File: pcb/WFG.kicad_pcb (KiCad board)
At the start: 2 copper layers, 54.1 x 30.5 mm, 32 parts, among them J1 Conn_01x02_Pin, J2 Conn_01x04_Socket, U1 LM324

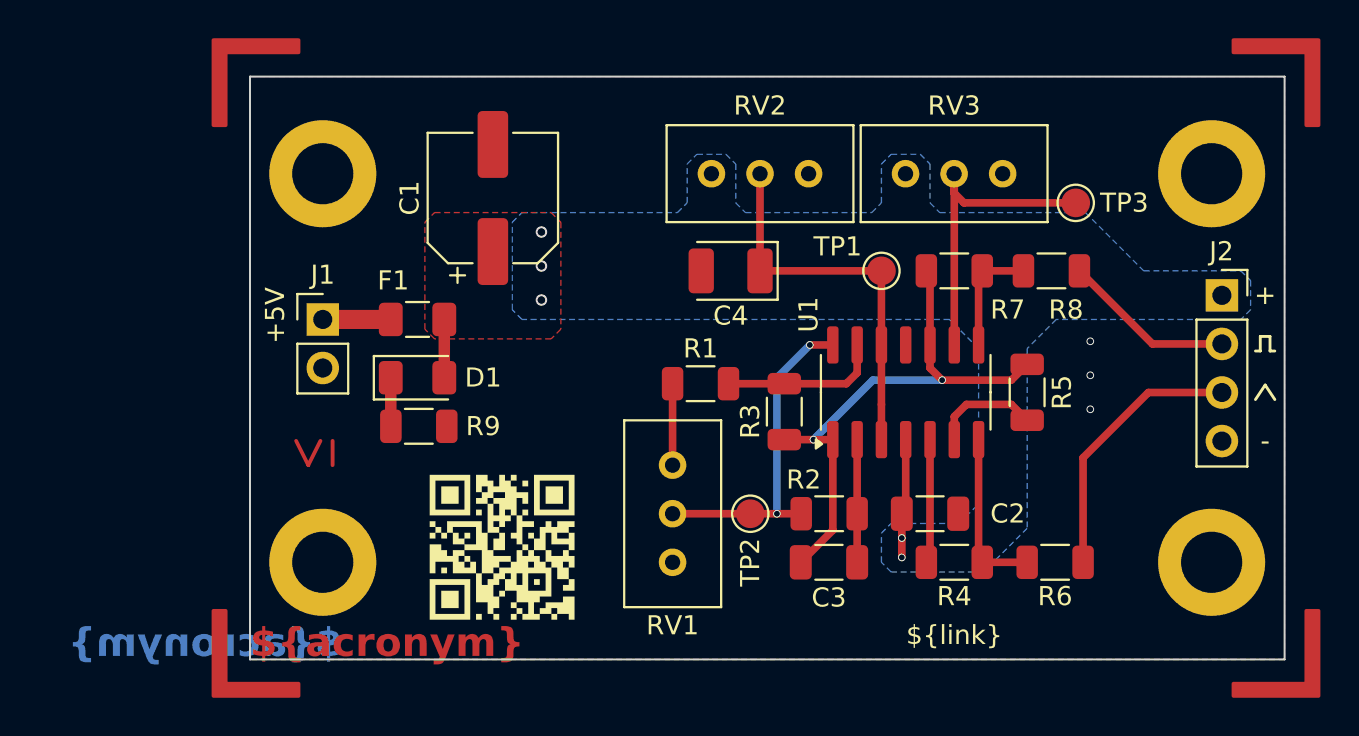
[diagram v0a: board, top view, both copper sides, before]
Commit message: Fix LM324 wiring
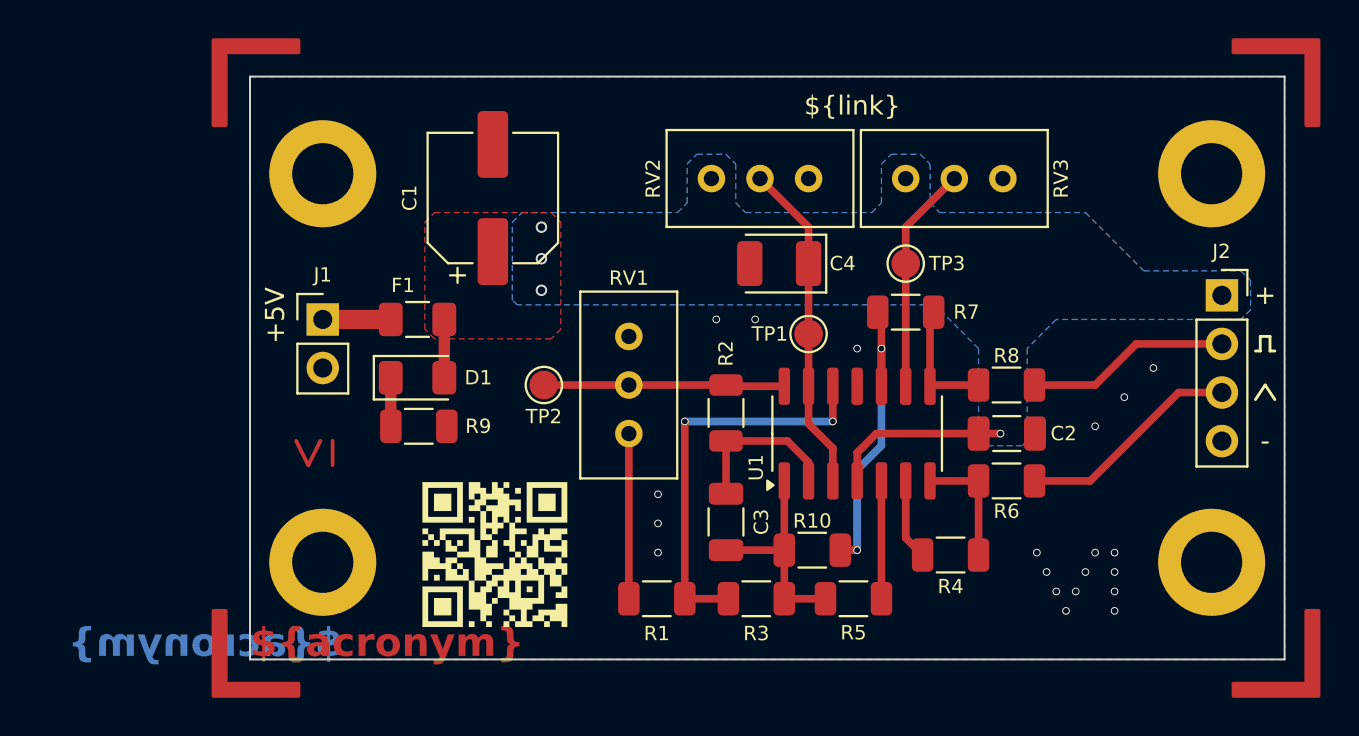
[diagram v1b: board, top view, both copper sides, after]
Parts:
- added R10: 1k, Resistor_SMD:R_1206_3216Metric, F.Cu at (152.6, 95.9)
- R7: value 1k -> 1Meg
- moved R5 14.1 mm to (154.8, 98.4), turned to 0 degrees
- moved TP2 12.7 mm to (138.6, 87.2)
- moved R1 11.5 mm to (144.5, 98.4)
- moved FID1 10.3 mm to (156.7, 97.3)
- moved R3 9.89 mm to (149.7, 98.4), turned to 180 degrees
- moved TP3 9.44 mm to (157.5, 80.9)
- moved FID2 8.76 mm to (162.8, 97.3)
- moved R2 7.54 mm to (148.1, 88.7), turned to 90 degrees
- moved R8 6.41 mm to (162.8, 87.2)
- moved C2 5.80 mm to (162.8, 89.8)
- moved C3 5.78 mm to (148.1, 94.4), turned to -90 degrees
- moved TP1 5.04 mm to (152.4, 84.6)
- moved R6 4.96 mm to (162.8, 92.3)
- moved U1 3.33 mm to (154.9, 89.8)
- moved R7 3.33 mm to (157.5, 83.4)
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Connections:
- C3 pad 2: Net-(U1C-+) -> Net-(C3-Pad2)
- R1 pad 1: Net-(U1D--) -> Net-(U1D-+)
- R3 pad 1: Net-(U1C-+) -> Net-(C3-Pad2)
- R3 pad 2: Net-(U1D--) -> Net-(U1D-+)
- R4 pad 1: Net-(U1B-+) -> Net-(U1B--)
- R5 pad 1: Net-(U1C-+) -> Net-(C3-Pad2)
- R5 pad 2: Net-(U1B--) -> Net-(U1B-+)
- U1 pad 1: Net-(U1C-+) -> Net-(C3-Pad2)
- U1 pad 12: Net-(U1A-+) -> Net-(U1D-+)
- U1 pad 13: Net-(U1D--) -> Net-(U1A-+)
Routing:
- net Net-(U1D-+): track 0.00 -> 21.1 mm, vias 0 -> 2
- net Net-(U1C-+): track 28.5 -> 17.2 mm
- net Net-(C3-Pad2): track 0.00 -> 10.9 mm
- net Net-(U1D--): track 8.42 -> 0.00 mm
- net Net-(U1C--): track 16.5 -> 11.3 mm
- net Net-(R2-Pad2): track 17.5 -> 12.6 mm, vias 2 -> 0
- net Net-(R1-Pad2): track 4.26 -> 8.64 mm
- net Net-(U1A-+): track 20.3 -> 16.8 mm
- net +5V: track 9.29 -> 12.2 mm, vias 5 -> 4
- net Net-(R4-Pad2): track 8.84 -> 6.41 mm
- net Net-(J2-Pin_3): track 14.1 -> 11.7 mm
- net Net-(U1A--): track 6.41 -> 8.52 mm
- net Net-(J2-Pin_2): track 9.03 -> 10.7 mm
- net Net-(U1B--): track 5.62 -> 4.24 mm
- net GND: vias 3 -> 20
